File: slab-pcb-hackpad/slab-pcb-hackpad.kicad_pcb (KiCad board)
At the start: 2 copper layers, 120 x 95 mm, 108 parts, among them J1 MagnetR, J2 MagnetL, J3 TRRS_R, J4 TRRS_L, J5 SSD1306, J6 Conn_01x06, Q1 MMBT3906, U1 Seeeduino Xiao rp2040, U2 PCA9555PW, U3 PCA9555PW

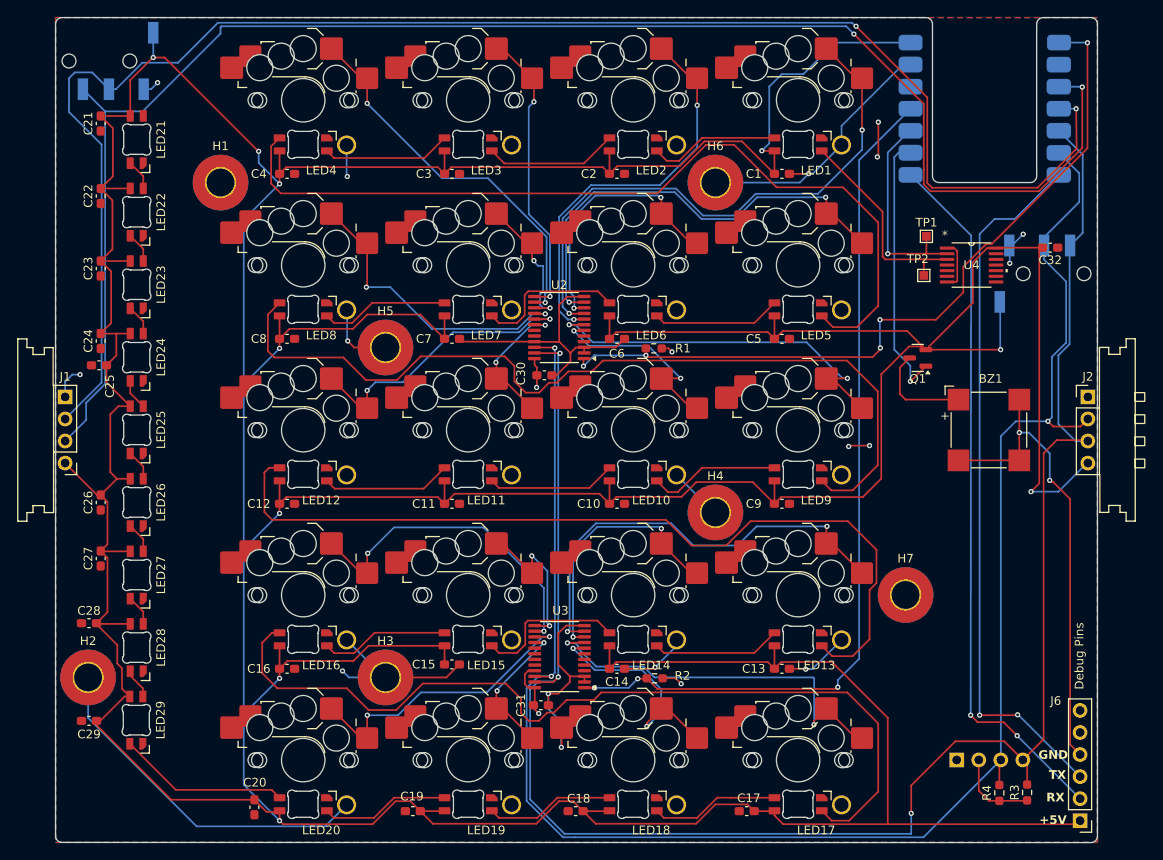
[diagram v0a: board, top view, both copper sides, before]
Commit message: feat: use slots instead of overlapped drill hits
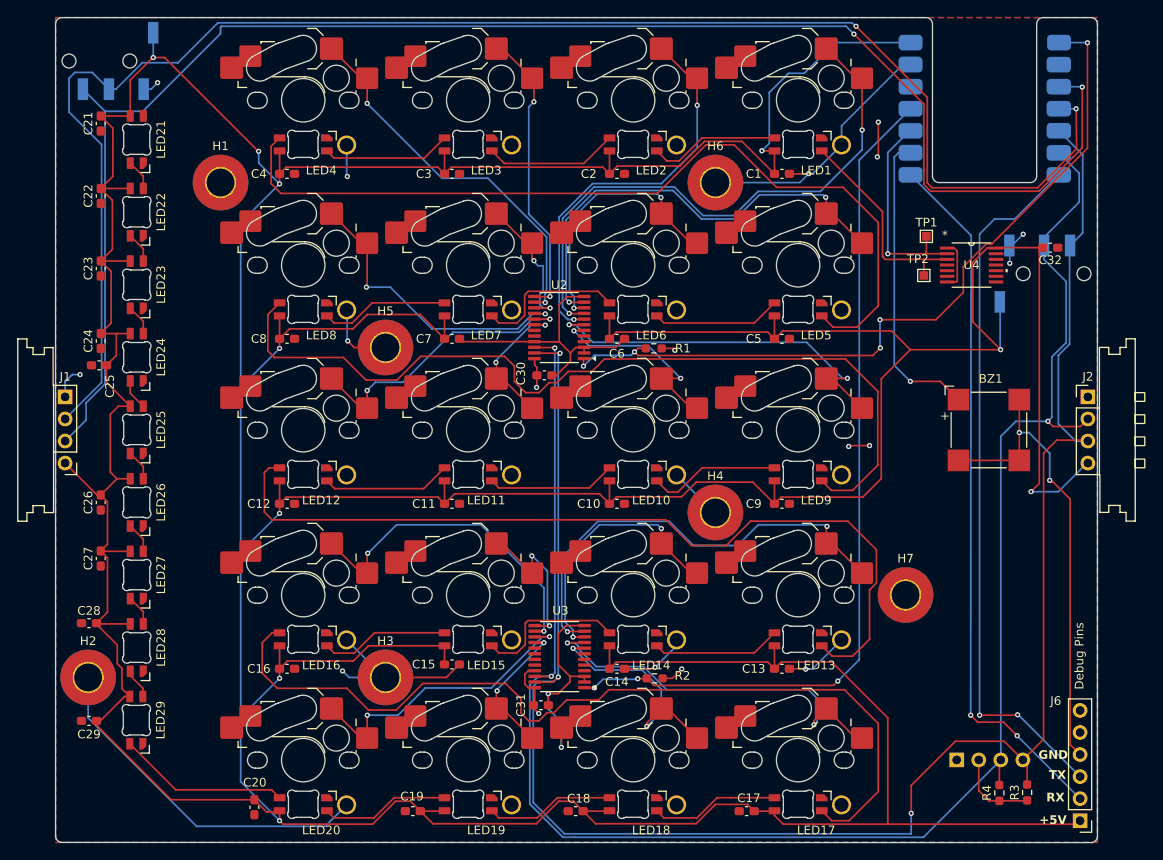
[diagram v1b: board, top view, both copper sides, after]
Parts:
- removed Q1: MMBT3906, Package_TO_SOT_SMD:SOT-23
- BZ1: footprint Buzzer_Beeper:MagneticBuzzer_CUI_CMT-8504-100-SMT -> CustomFootprints:buzzer
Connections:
- BZ1 pad 1: Net-(BZ1-+) -> /BUZZER
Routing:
- net Net-(BZ1-+): track 11.6 -> 0.00 mm
- net /BUZZER: track 31.2 -> 35.1 mm
- net VBUS: track 795.1 -> 793.1 mm
- net /KEY14: track 29.8 -> 30.7 mm
- net /KEY13: track 51.8 -> 52.7 mm
- net /KEY17: track 45.4 -> 44.6 mm
- net /EXPANDER1_INT: track 89.7 -> 90.5 mm
- net /EXPANDER2_INT: track 100.4 -> 99.7 mm
- net +3V3: track 30.3 -> 30.8 mm

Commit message: chore: move via outside of text
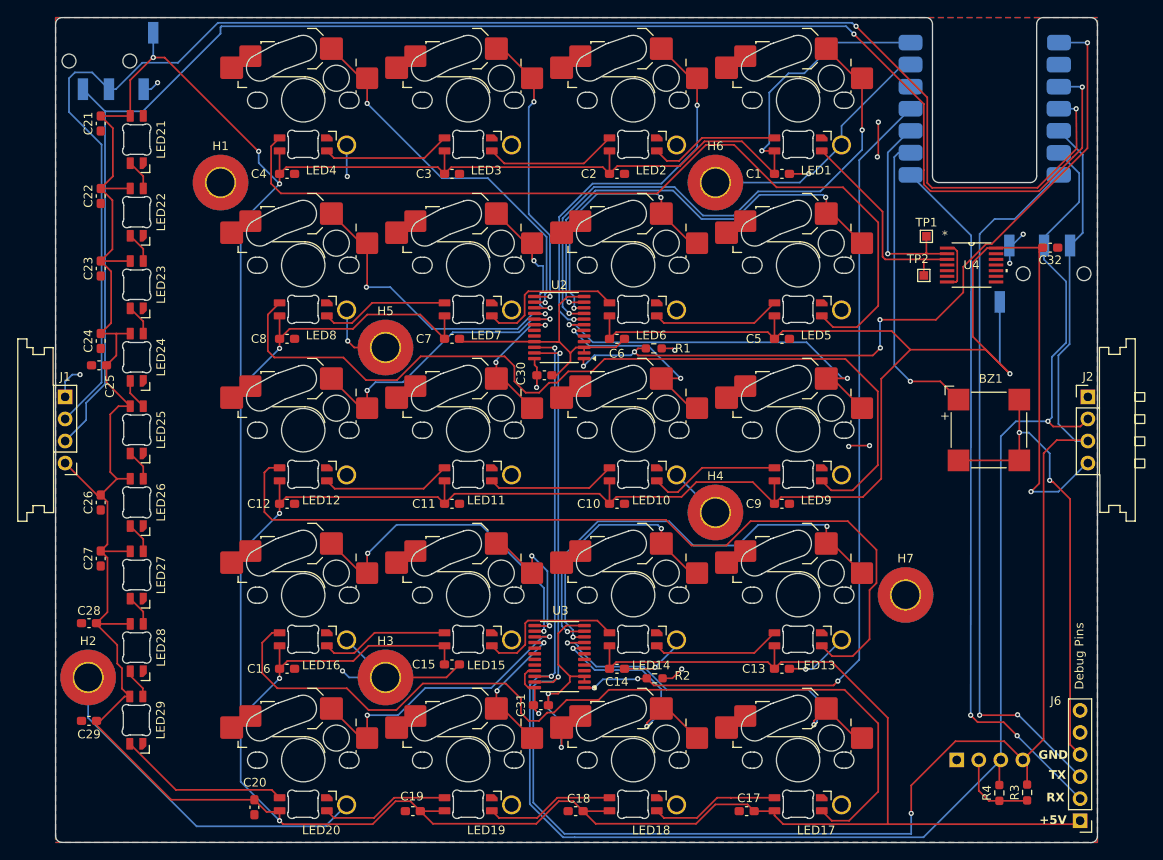
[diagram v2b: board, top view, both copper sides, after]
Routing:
- net VBUS: track 793.1 -> 801.7 mm

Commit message: feat: bump to 3.2
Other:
- board text added: "version 3.2 'nowhere'"
- board text removed: "version 3.1 'nowhere'"
